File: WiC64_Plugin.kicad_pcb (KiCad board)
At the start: 2 copper layers, 54.4 x 63.7 mm, 59 parts, among them CN1 USERPORT-C64, CN2 OLED0.96, Q1 BSS138, Q10 BSS138, Q11 BSS138, Q2 BSS138, Q3 BSS138, Q4 BSS138, Q5 BSS138, Q6 BSS138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

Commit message: Initial +4 version
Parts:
- CN1: value USERPORT-C64 -> PLUS4_USERPORT
- SW1: value RESET-C64 -> RESET
- moved JP1 1.88 mm to (160.2, 102.8)
- moved JP2 1.27 mm to (153.4, 125.6)
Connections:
- CN1 pad 4: unconnected-(CN1-CNT-Pad4) -> /PB2
- CN1 pad 5: unconnected-(CN1-SP1-Pad5) -> /PB3
- CN1 pad 6: unconnected-(CN1-CNT2-Pad6) -> /PB4
- CN1 pad 7: unconnected-(CN1-SP2-Pad7) -> /PB5
- CN1 pad 8: /PC2 -> unconnected-(CN1-RXC-Pad8)
- CN1 pad B: /FLAG2 -> /PB0
- CN1 pad C: /PB0 -> unconnected-(CN1-RXD-PadC)
- CN1 pad D: /PB1 -> /PA2
- CN1 pad E: /PB2 -> /PC2
- CN1 pad F: /PB3 -> /PB7
- CN1 pad H: /PB4 -> /FLAG2
- CN1 pad J: /PB5 -> /PB6
- CN1 pad K: /PB6 -> /PB1
- CN1 pad L: /PB7 -> unconnected-(CN1-~{DSR}-PadL)
- CN1 pad M: /PA2 -> unconnected-(CN1-TXD-PadM)
- Q1 pad 2: /IO26 -> /IO16
- Q1 pad 3: /FLAG2 -> /PB0
- Q10 pad 2: /IO25 -> /IO23
- Q10 pad 3: /PB7 -> /PB6
- Q11 pad 2: /IO27 -> /IO17
- Q11 pad 3: /PA2 -> /PB1
- Q2 pad 2: /IO16 -> /IO18
- Q2 pad 3: /PB0 -> /PB2
- Q3 pad 2: /IO17 -> /IO27
- Q3 pad 3: /PB1 -> /PA2
- Q4 pad 2: /IO18 -> /IO14
- Q4 pad 3: /PB2 -> /PC2
- Q6 pad 2: /IO21 -> /IO25
- Q6 pad 3: /PB4 -> /PB7
- Q7 pad 2: /IO14 -> /IO21
- Q7 pad 3: /PC2 -> /PB4
- Q8 pad 2: /IO22 -> /IO26
- Q8 pad 3: /PB5 -> /FLAG2
- Q9 pad 2: /IO23 -> /IO22
- Q9 pad 3: /PB6 -> /PB5
- R1 pad 2: /IO26 -> /IO16
- R11 pad 2: /IO21 -> /IO25
- R12 pad 2: /PB4 -> /PB7
- R13 pad 2: /IO14 -> /IO21
- R14 pad 2: /PC2 -> /PB4
- R15 pad 2: /IO22 -> /IO26
- R16 pad 2: /PB5 -> /FLAG2
- R17 pad 2: /IO23 -> /IO22
- R18 pad 2: /PB6 -> /PB5
- R19 pad 2: /IO25 -> /IO23
- R2 pad 2: /FLAG2 -> /PB0
- R20 pad 2: /PB7 -> /PB6
- R21 pad 2: /IO27 -> /IO17
- R22 pad 2: /PA2 -> /PB1
- R3 pad 2: /IO16 -> /IO18
- R4 pad 2: /PB0 -> /PB2
- R5 pad 2: /IO17 -> /IO27
- R6 pad 2: /PB1 -> /PA2
- R7 pad 2: /IO18 -> /IO14
- R8 pad 2: /PB2 -> /PC2
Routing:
- net /IO26: track 57.4 -> 30.8 mm, vias 1 -> 2
- net /IO17: track 20.3 -> 40.1 mm
- net /IO14: track 22.4 -> 37.1 mm, vias 1 -> 2
- net /IO16: track 21.4 -> 29.6 mm
- net /IO18: track 21.6 -> 29.2 mm
- net /PB4: track 25.8 -> 20.3 mm, vias 0 -> 1
- net /IO27: track 39.3 -> 44.7 mm, vias 1 -> 2
- net /SCL: track 44.3 -> 39.4 mm
- net /PB7: track 21.8 -> 25.7 mm
- net /IO22: track 19.2 -> 15.2 mm
- net /IO23: track 17.8 -> 14.0 mm
- net /PB2: track 22.7 -> 25.4 mm, vias 0 -> 1
- net /SW2C: track 77.5 -> 79.9 mm
- net +3.3V: track 130.1 -> 132.2 mm, vias 9 -> 8
- net /PB3: track 22.7 -> 24.5 mm, vias 0 -> 1
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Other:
- board text added: "WiC +4"
- board text removed: "WiC 64"

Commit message: Complete changes for +4 version
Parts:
- added L1: FERRITE, WiC64:Ferrite_D6.0mm_L10.00mm_Horizontal, F.Cu at (163.7, 125.5)
- moved C2 5.41 mm to (158.8, 128.5)
- moved D3 2.54 mm to (157.2, 124.3)
- moved C1 0.63 mm to (146.2, 125.1), turned to 180 degrees
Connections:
- CN1 pad 2: +5V -> Net-(CN1-VCC)
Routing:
- net Net-(CN1-VCC): track 0.00 -> 11.7 mm, vias 0 -> 1
- net +5V: track 102.7 -> 92.6 mm, vias 13 -> 12
- net /PB2: track 25.4 -> 30.9 mm
- net /SDA: track 58.2 -> 63.2 mm
- net /PA2: track 24.7 -> 27.5 mm
- net /IO14: track 37.1 -> 38.7 mm
- net VCC: track 61.1 -> 62.8 mm
- net /IO25: track 37.3 -> 38.8 mm
- net /IO27: track 44.7 -> 46.0 mm
- net /PC2: track 22.7 -> 23.7 mm
- net /IO26: track 30.8 -> 31.7 mm
- net Net-(D4-+): track 12.3 -> 11.4 mm
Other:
- board text added: "FUNCTION"
- board text added: "The Commodore 16/+4 Wireless Interface Card"
- board text added: "V1"
- board text added: "©2024 SukkoPera, based on WiC64, ©2021 GMP - CC-BY-4.0"
- board text removed: "Original PCB-Design (C) 2021 by GMP"
- board text removed: "Rev. 0.6-Sukko"
- board text removed: "The Commodore 64 Wireless Interface Card"

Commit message: Move SCL/SDA tracks around
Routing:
- net /SCL: track 39.4 -> 44.5 mm
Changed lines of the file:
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@@
 	)
 	(segment
-		(start 148.7297 80.6958)
-		(end 148.7297 113.3475)
+		(start 153.67 120.1928)
+		(end 157.226 120.1928)
 		(width 0.25)
 		(layer "F.Cu")
@@
 	)
 	(segment
-		(start 148.3228 80.2889)
-		(end 148.7297 80.6958)
+		(start 148.717 113.3348)
+		(end 150.749 115.3668)
 		(width 0.25)
 		(layer "F.Cu")
@@
 	)
 	(segment
-		(start 150.749 117.2718)
-		(end 153.67 120.1928)
+		(start 148.717 80.6831)
+		(end 148.717 113.3348)
 		(width 0.25)
 		(layer "F.Cu")
@@
 	)
 	(segment
-		(start 157.226 120.1928)
-		(end 158.496 121.4628)
+		(start 158.496 121.4628)
+		(end 158.496 124.7648)
 		(width 0.25)
 		(layer "F.Cu")
@@
 	)
 	(segment
-		(start 158.496 124.7648)
-		(end 157.734 125.5268)
+		(start 148.3228 80.2889)
+		(end 148.717 80.6831)
 		(width 0.25)
 		(layer "F.Cu")
@@
 	)
 	(segment
-		(start 153.67 120.1928)
-		(end 157.226 120.1928)
+		(start 157.226 120.1928)
+		(end 158.496 121.4628)
 		(width 0.25)
 		(layer "F.Cu")
@@
 	)
 	(segment
-		(start 148.7297 113.3475)
-		(end 150.749 115.3668)
+		(start 150.749 117.2718)
+		(end 153.67 120.1928)
 		(width 0.25)
 		(layer "F.Cu")
@@
 	)
 	(segment
-		(start 158.496 121.4628)
-		(end 158.496 124.7648)
+		(start 158.496 124.7648)
+		(end 157.734 125.5268)
 		(width 0.25)
 		(layer "F.Cu")
@@
 	)
 	(segment
-		(start 151.13 101.2698)
-		(end 151.13 79.9338)
+		(start 151.257 105.9688)
+		(end 151.257 107.8738)
 		(width 0.25)
 		(layer "F.Cu")
@@
 	)
 	(segment
-		(start 151.13 79.9338)
+		(start 151.257 107.8738)
+		(end 151.892 108.5088)
+		(width 0.25)
+		(layer "F.Cu")
+		(net 33)
+	)
+	(segment
+		(start 151.892 108.5088)
+		(end 158.5468 108.5088)
+		(width 0.25)
+		(layer "F.Cu")
+		(net 33)
+	)
+	(segment
+		(start 147.0192 77.7748)
 		(end 148.971 77.7748)
 		(width 0.25)
@@
 	)
 	(segment
-		(start 160.1216 106.934)
-		(end 157.3784 104.1908)
+		(start 149.606 78.4098)
+		(end 149.606 104.3178)
 		(width 0.25)
 		(layer "F.Cu")
@@
 	)
 	(segment
-		(start 154.051 104.1908)
-		(end 151.13 101.2698)
-		(width 0.25)
-		(layer "F.Cu")
-		(net 33)
-	)
-	(segment
-		(start 157.3784 104.1908)
-		(end 154.051 104.1908)
-		(width 0.25)
-		(layer "F.Cu")
-		(net 33)
-	)
-	(segment
-		(start 147.0192 77.7748)
-		(end 145.7828 79.0112)
+		(start 158.5468 108.5088)
+		(end 160.1216 106.934)
 		(width 0.25)
 		(layer "F.Cu")
@@
 	(segment
 		(start 148.971 77.7748)
+		(end 149.606 78.4098)
+		(width 0.25)
+		(layer "F.Cu")
+		(net 33)
+	)
+	(segment
+		(start 145.7828 79.0112)
 		(end 147.0192 77.7748)
 		(width 0.25)
 		(layer "F.Cu")
+		(net 33)
+	)
+	(segment
+		(start 149.606 104.3178)
+		(end 151.257 105.9688)
+		(width 0.25)
+		(layer "F.Cu")

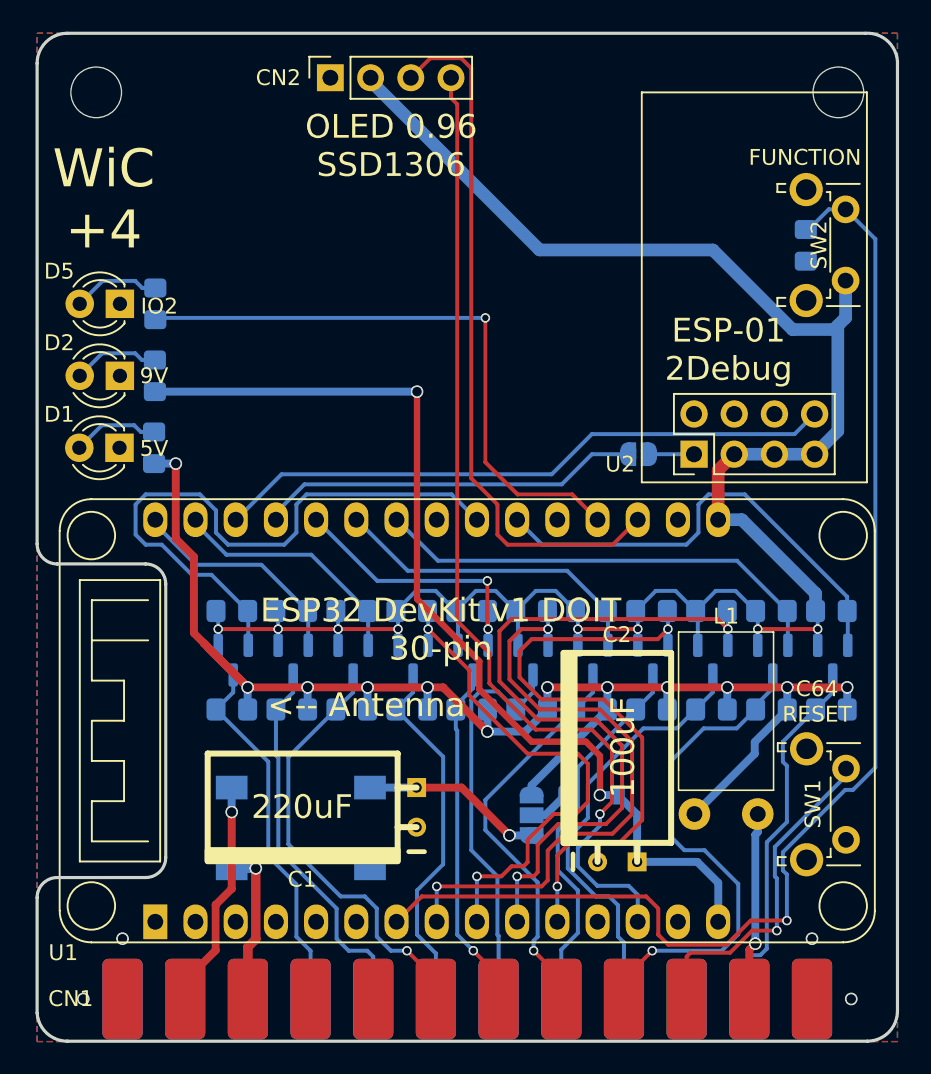
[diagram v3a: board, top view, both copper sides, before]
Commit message: Latch FLAG2
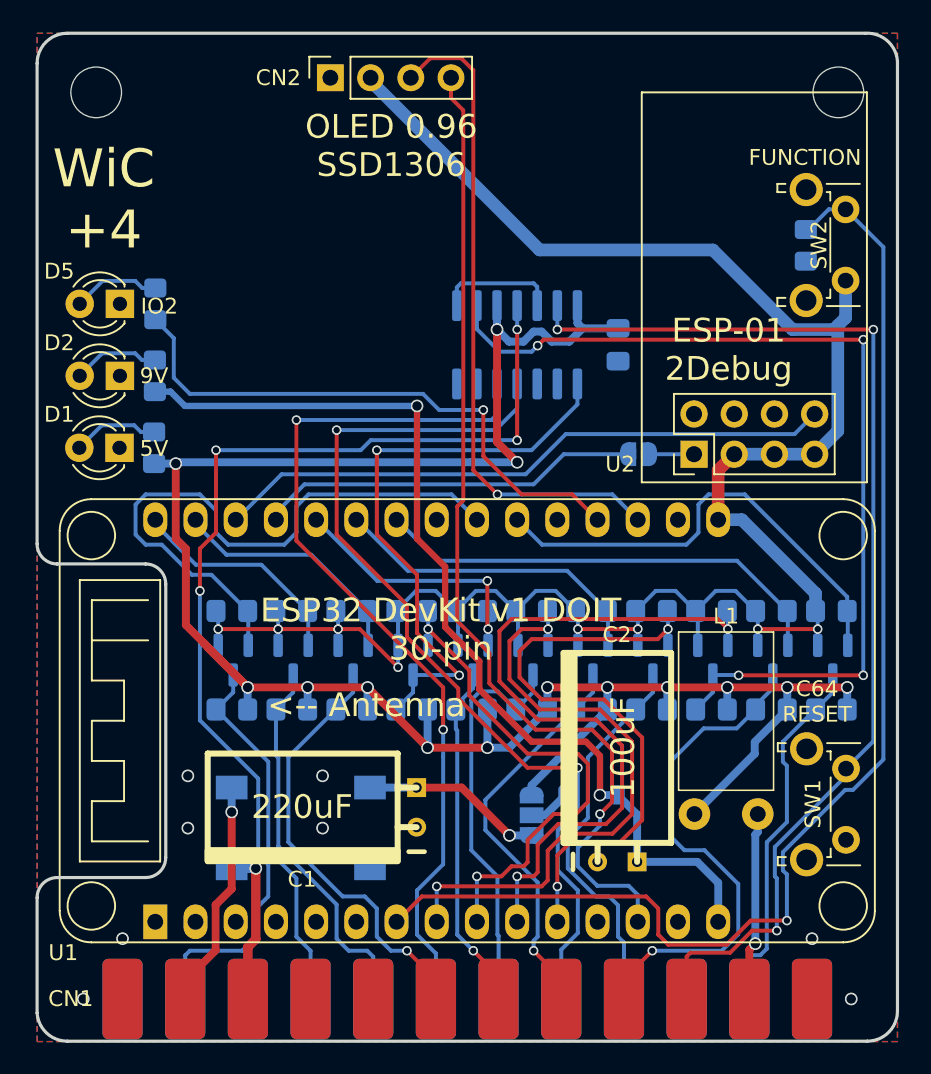
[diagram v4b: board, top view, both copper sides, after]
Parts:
- added C3: 100n, Capacitor_SMD:C_0805_2012Metric_Pad1.18x1.45mm_HandSolder, B.Cu at (158.9, 95.9)
- added U3: 74HCT74, Package_SO:SOIC-14_3.9x8.7mm_P1.27mm, B.Cu at (152.5, 95.9)
- added V5: SukkoPera, WiC64:PearLogo, B.Cu at (147.4, 101.7)
- moved V1 3.15 mm to (140.8, 93.4)
- moved V2 2.15 mm to (164.1, 93.4)
- renumbered V5 to V6
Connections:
- net Net-(CN1-~{RESET}) renamed /~{RESET}
- CN1 pad D: /PA2 -> /PC2
- CN1 pad E: /PC2 -> /FLAG2_CLEAR
- CN1 pad H: /FLAG2 -> /FLAG2_LATCHED
- CN1 pad M: unconnected-(CN1-TXD-PadM) -> /PA2_TOGGLE
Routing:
- net /PA2_TOGGLE: track 0.00 -> 68.5 mm, vias 0 -> 4
- net /FLAG2_CLEAR: track 0.00 -> 58.7 mm, vias 0 -> 2
- net /FLAG2_LATCHED: track 0.00 -> 56.1 mm, vias 0 -> 2
- net /~{RESET}: track 20.7 -> 70.6 mm, vias 1 -> 3
- net +5V: track 92.6 -> 137.6 mm, vias 12 -> 14
- net /PA2: track 27.5 -> 60.2 mm, vias 0 -> 4
- net /FLAG2: track 23.3 -> 36.8 mm, vias 0 -> 2
- net Net-(U3B-D): track 0.00 -> 7.61 mm
- net /SCL: track 44.5 -> 41.7 mm, vias 0 -> 1
- net +3.3V: track 132.2 -> 134.6 mm
- net /IO2: track 38.6 -> 36.4 mm
- net /PC2: track 23.7 -> 24.7 mm
- net VCC: track 62.8 -> 62.3 mm
- net GND: vias 4 -> 8
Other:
- board text added: "Commodore 16/+4 Wireless Interface Card"
- board text added: "SukkoPera"
- board text added: "github.com/SukkoPera/WiC64-Plus4 Original Project: www.wic64.com"
- board text removed: "The Commodore 16/+4 Wireless Interface Card"
- board text removed: "https://www.wic64.com"
